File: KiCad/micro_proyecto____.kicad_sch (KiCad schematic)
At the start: 37 parts, among them J1 Conn_01x02, J2 Conn_01x05, J3 Conn_01x02, J4 Conn_01x02, J5 Conn_01x02, J6 Conn_01x02, SW1 SW_Push, SW2 SW_Push, SW3 SW_Push, SW4 SW_Push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

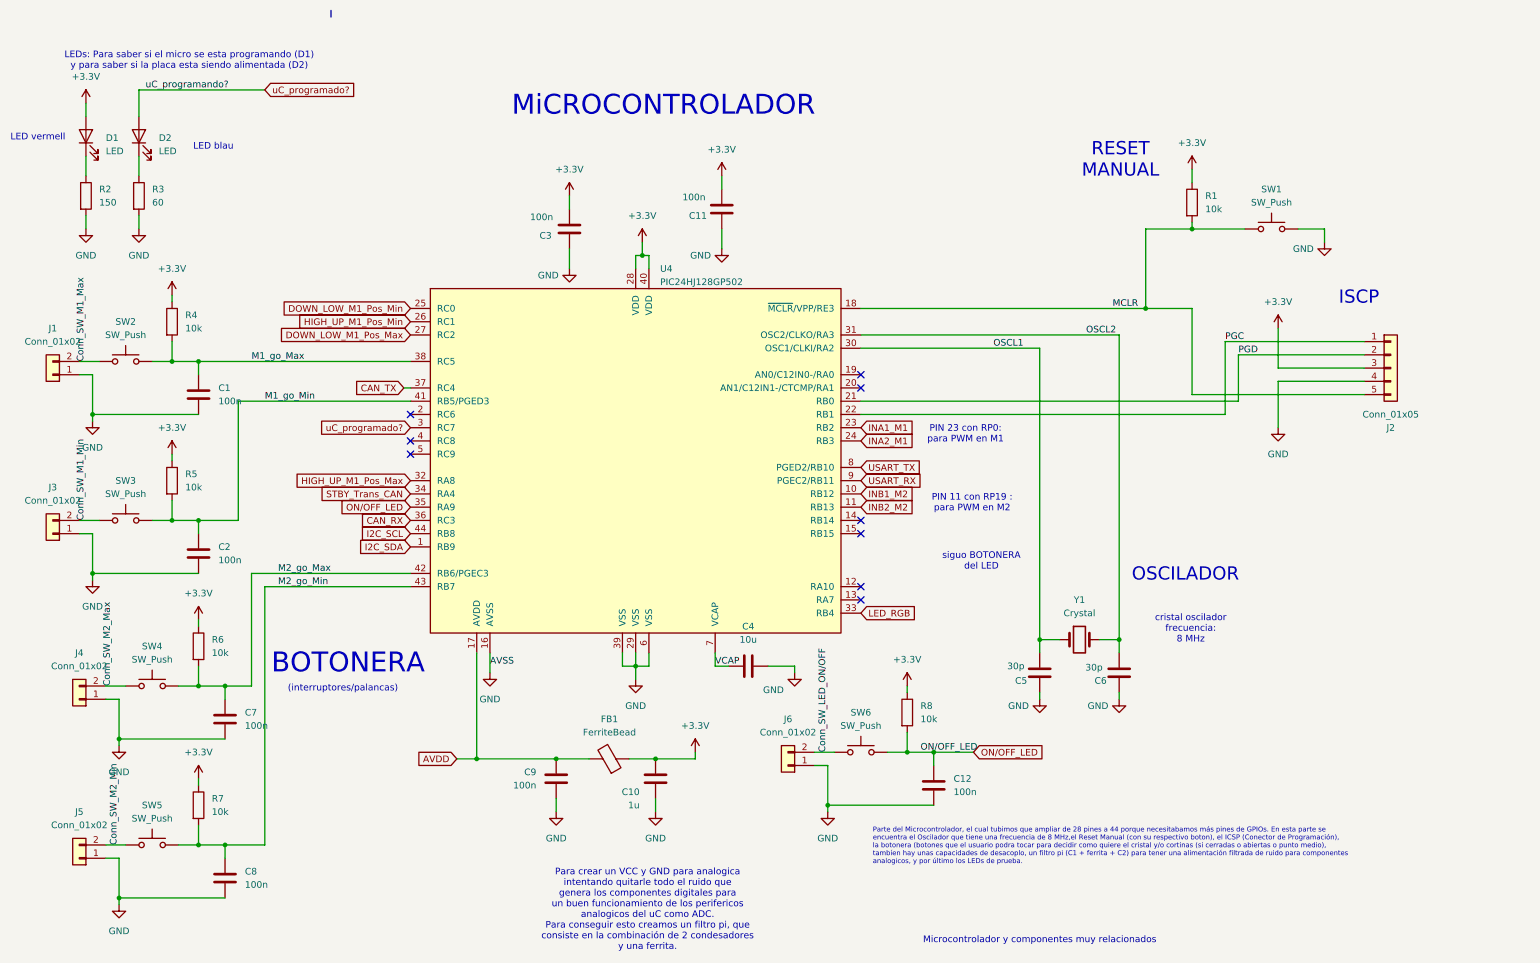
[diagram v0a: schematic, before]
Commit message: Layout con pocos cables en capa Bot pero todavai hay que hacer cambios que nos dijo el Miercoles pasado
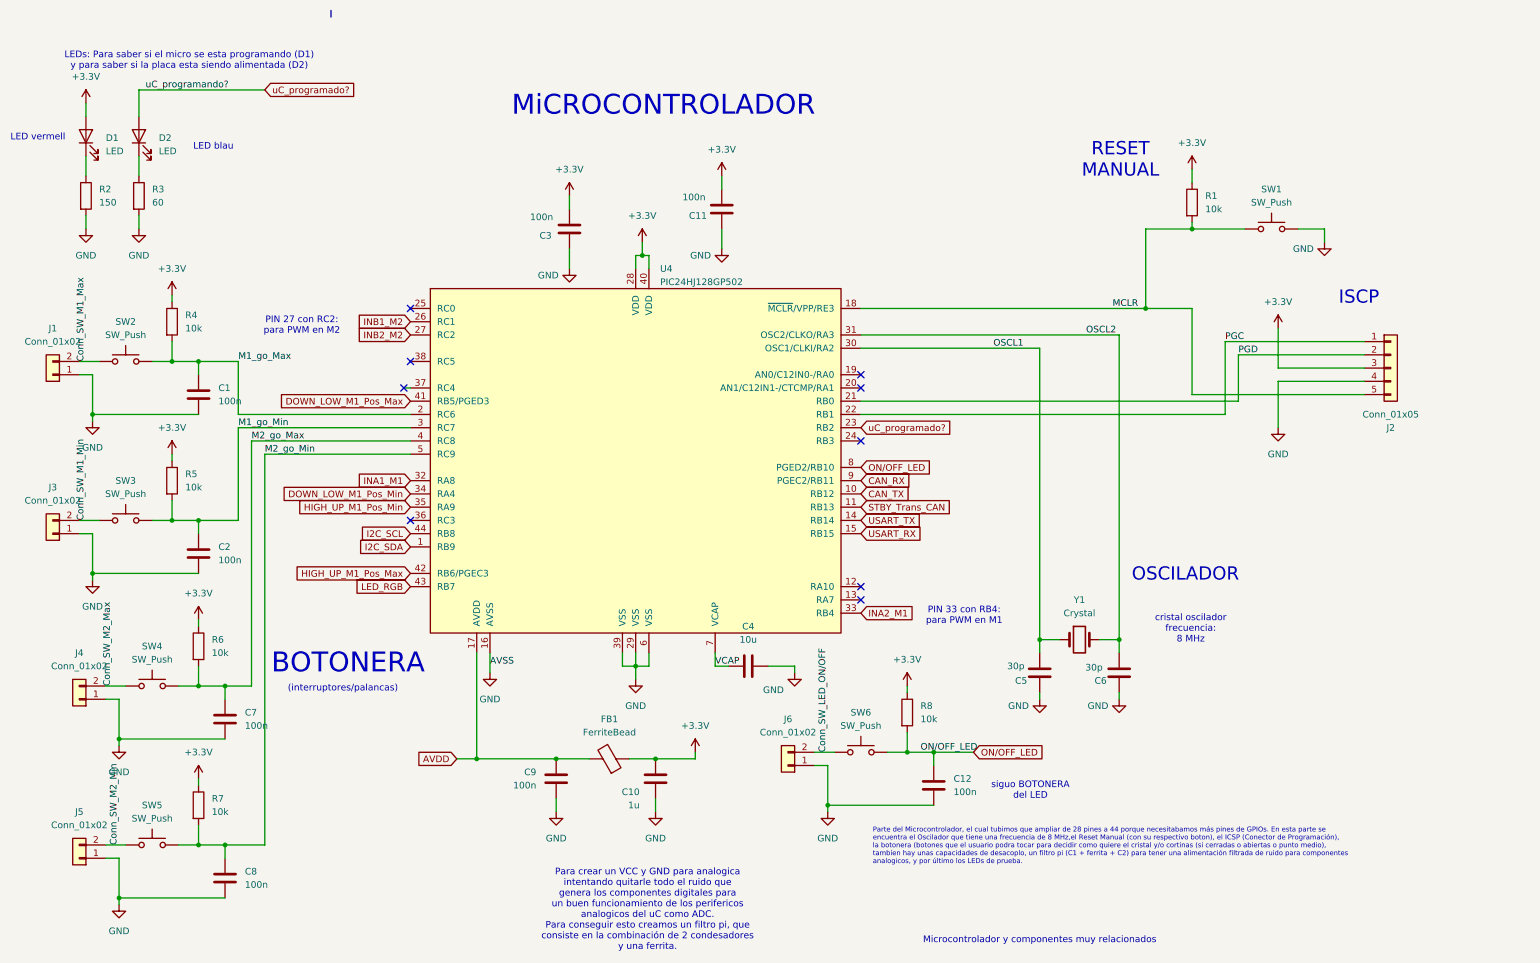
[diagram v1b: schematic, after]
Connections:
- net CAN_RX: now also U4.9 (PGEC2/RB11); no longer U4.36 (RC3)
- net CAN_TX: now also U4.10 (RB12); no longer U4.37 (RC4)
- net DOWN_LOW_M1_Pos_Max: now also U4.41 (RB5/PGED3); no longer U4.27 (RC2)
- net DOWN_LOW_M1_Pos_Min: now also U4.34 (NC); no longer U4.25 (RC0)
- net HIGH_UP_M1_Pos_Max: now also U4.42 (RB6/PGEC3); no longer U4.32 (RA8)
- net HIGH_UP_M1_Pos_Min: now also U4.35 (RA9); no longer U4.26 (RC1)
- net INA1_M1: now also U4.32 (RA8); no longer U4.23 (RB2)
- net INA2_M1: now also U4.33 (RB4); no longer U4.24 (RB3)
- net INB1_M2: now also U4.26 (RC1); no longer U4.10 (RB12)
- net INB2_M2: now also U4.27 (RC2); no longer U4.11 (RB13)
- net LED_RGB: now also U4.43 (RB7); no longer U4.33 (RB4)
- net M1_go_Max: now also U4.2 (RC6); no longer U4.38 (RC5)
- net M1_go_Min: now also U4.3 (RC7); no longer U4.41 (RB5/PGED3)
- net M2_go_Max: now also U4.4 (RC8); no longer U4.42 (RB6/PGEC3)
- net M2_go_Min: now also U4.5 (RC9); no longer U4.43 (RB7)
- net ON/OFF_LED: now also U4.8 (PGED2/RB10); no longer U4.35 (RA9)
- net STBY_Trans_CAN: now also U4.11 (RB13); no longer U4.34 (NC)
- net USART_RX: now also U4.15 (RB15); no longer U4.9 (PGEC2/RB11)
- net USART_TX: now also U4.14 (RB14); no longer U4.8 (PGED2/RB10)
- net uC_programado?: now also U4.23 (RB2); no longer U4.3 (RC7)
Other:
- note added: "PIN 27 con RC2: para PWM en M2"
- note added: "PIN 33 con RB4: para PWM en M1"
- note removed: "PIN 11 con RP19 : para PWM en M2"
- note removed: "PIN 23 con RP0: para PWM en M1"

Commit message: Cambios Layout propuestos para mejorar posicionamiento
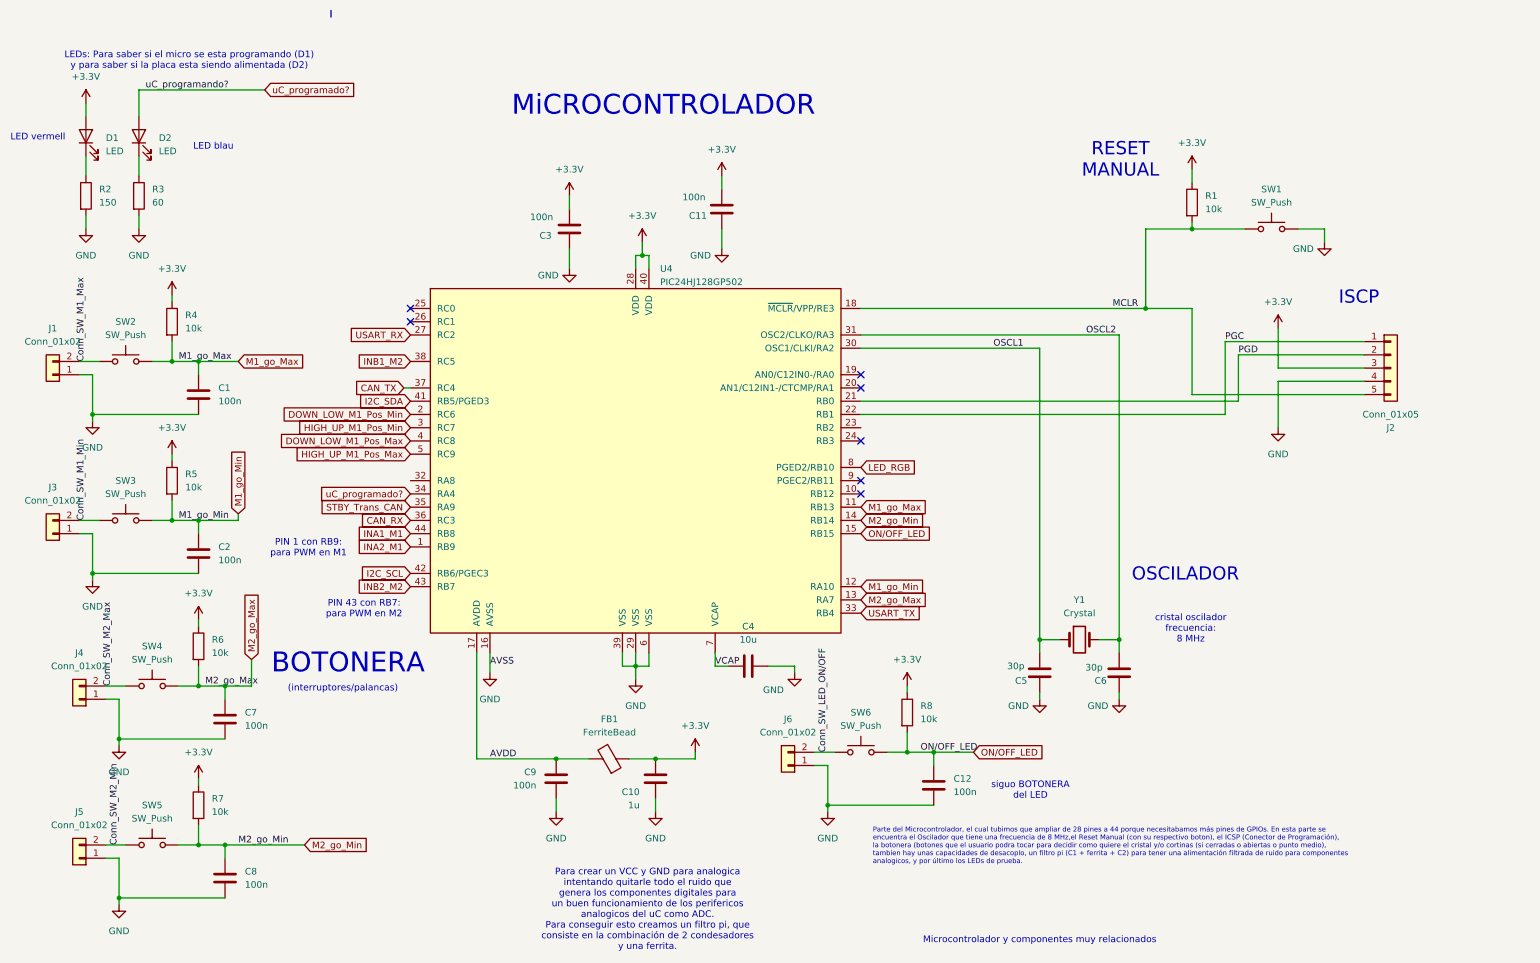
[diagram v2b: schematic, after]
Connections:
- net CAN_RX: now also U4.36 (RC3); no longer U4.9 (PGEC2/RB11)
- net CAN_TX: now also U4.37 (RC4); no longer U4.10 (RB12)
- net DOWN_LOW_M1_Pos_Max: now also U4.4 (RC8); no longer U4.41 (RB5/PGED3)
- net DOWN_LOW_M1_Pos_Min: now also U4.2 (RC6); no longer U4.34 (NC)
- net HIGH_UP_M1_Pos_Max: now also U4.5 (RC9); no longer U4.42 (RB6/PGEC3)
- net HIGH_UP_M1_Pos_Min: now also U4.3 (RC7); no longer U4.35 (RA9)
- net I2C_SCL: now also U4.42 (RB6/PGEC3); no longer U4.44 (RB8)
- net I2C_SDA: now also U4.41 (RB5/PGED3); no longer U4.1 (RB9)
- net INA1_M1: now also U4.44 (RB8); no longer U4.32 (RA8)
- net INA2_M1: now also U4.1 (RB9); no longer U4.33 (RB4)
- net INB1_M2: now also U4.38 (RC5); no longer U4.26 (RC1)
- net INB2_M2: now also U4.43 (RB7); no longer U4.27 (RC2)
- net LED_RGB: now also U4.8 (PGED2/RB10); no longer U4.43 (RB7)
- net M1_go_Max: now also U4.11 (RB13); no longer U4.2 (RC6)
- net M1_go_Min: now also U4.12 (RA10); no longer U4.3 (RC7)
- net M2_go_Max: now also U4.13 (RA7); no longer U4.4 (RC8)
- net M2_go_Min: now also U4.14 (RB14); no longer U4.5 (RC9)
- net ON/OFF_LED: now also U4.15 (RB15); no longer U4.8 (PGED2/RB10)
- net STBY_Trans_CAN: now also U4.35 (RA9); no longer U4.11 (RB13)
- net USART_RX: now also U4.27 (RC2); no longer U4.15 (RB15)
- net USART_TX: now also U4.33 (RB4); no longer U4.14 (RB14)
- net uC_programado?: now also U4.34 (NC); no longer U4.23 (RB2)
- no-connect marks 9 -> 7
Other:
- note added: "PIN 1 con RB9: para PWM en M1"
- note added: "PIN 43 con RB7: para PWM en M2"
- note removed: "PIN 27 con RC2: para PWM en M2"
- note removed: "PIN 33 con RB4: para PWM en M1"

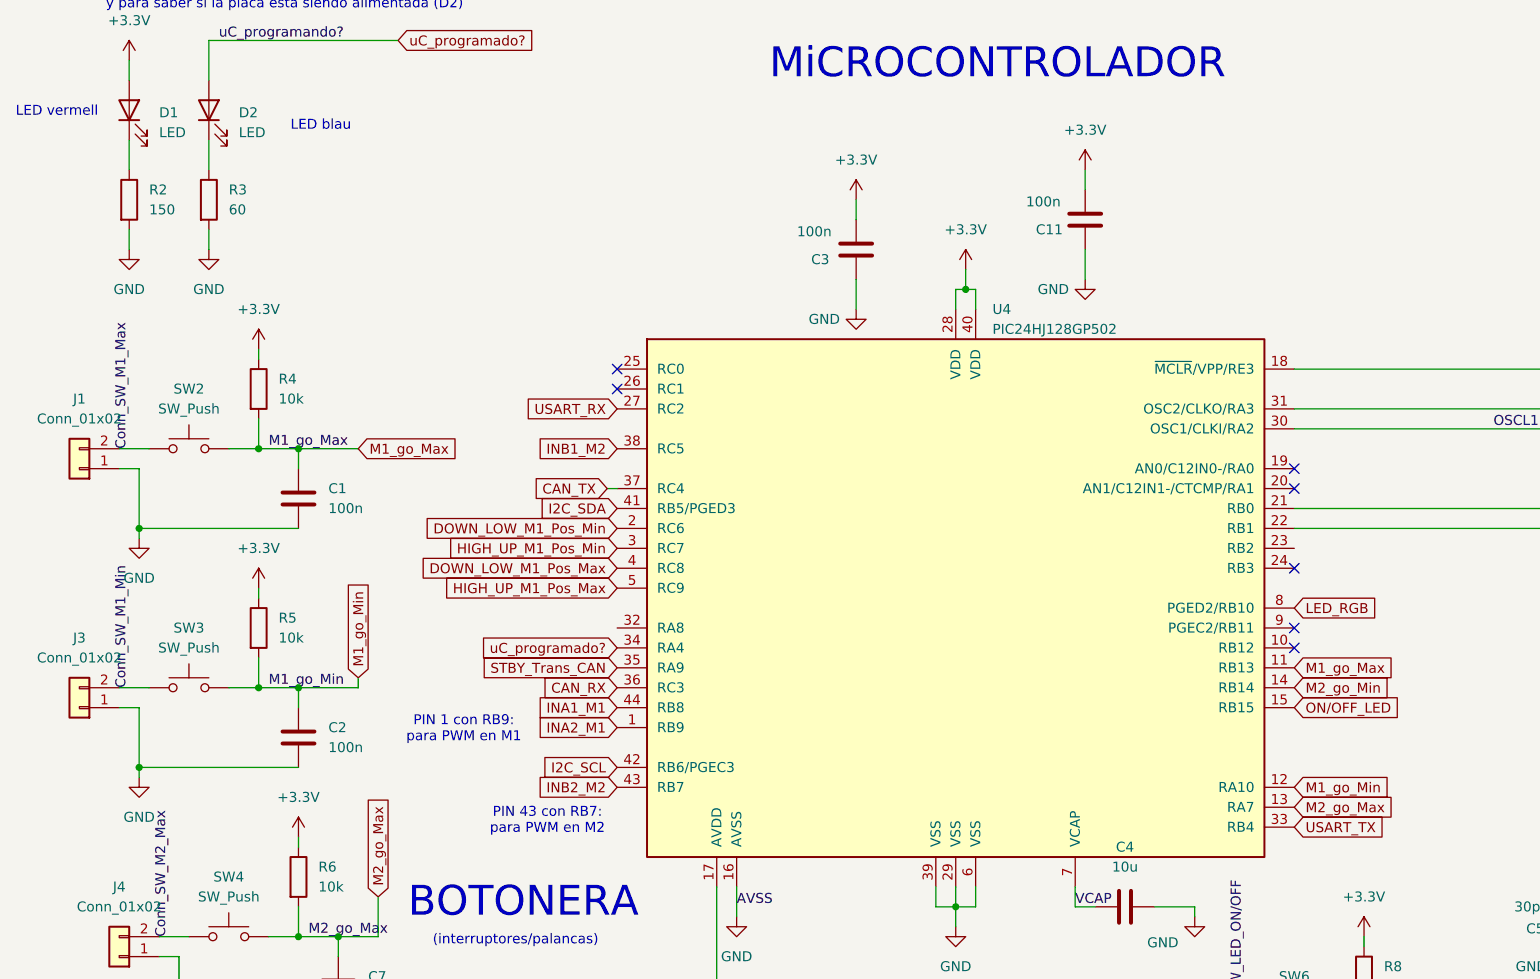
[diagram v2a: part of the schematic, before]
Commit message: Arreglo de algunos fallos DRC
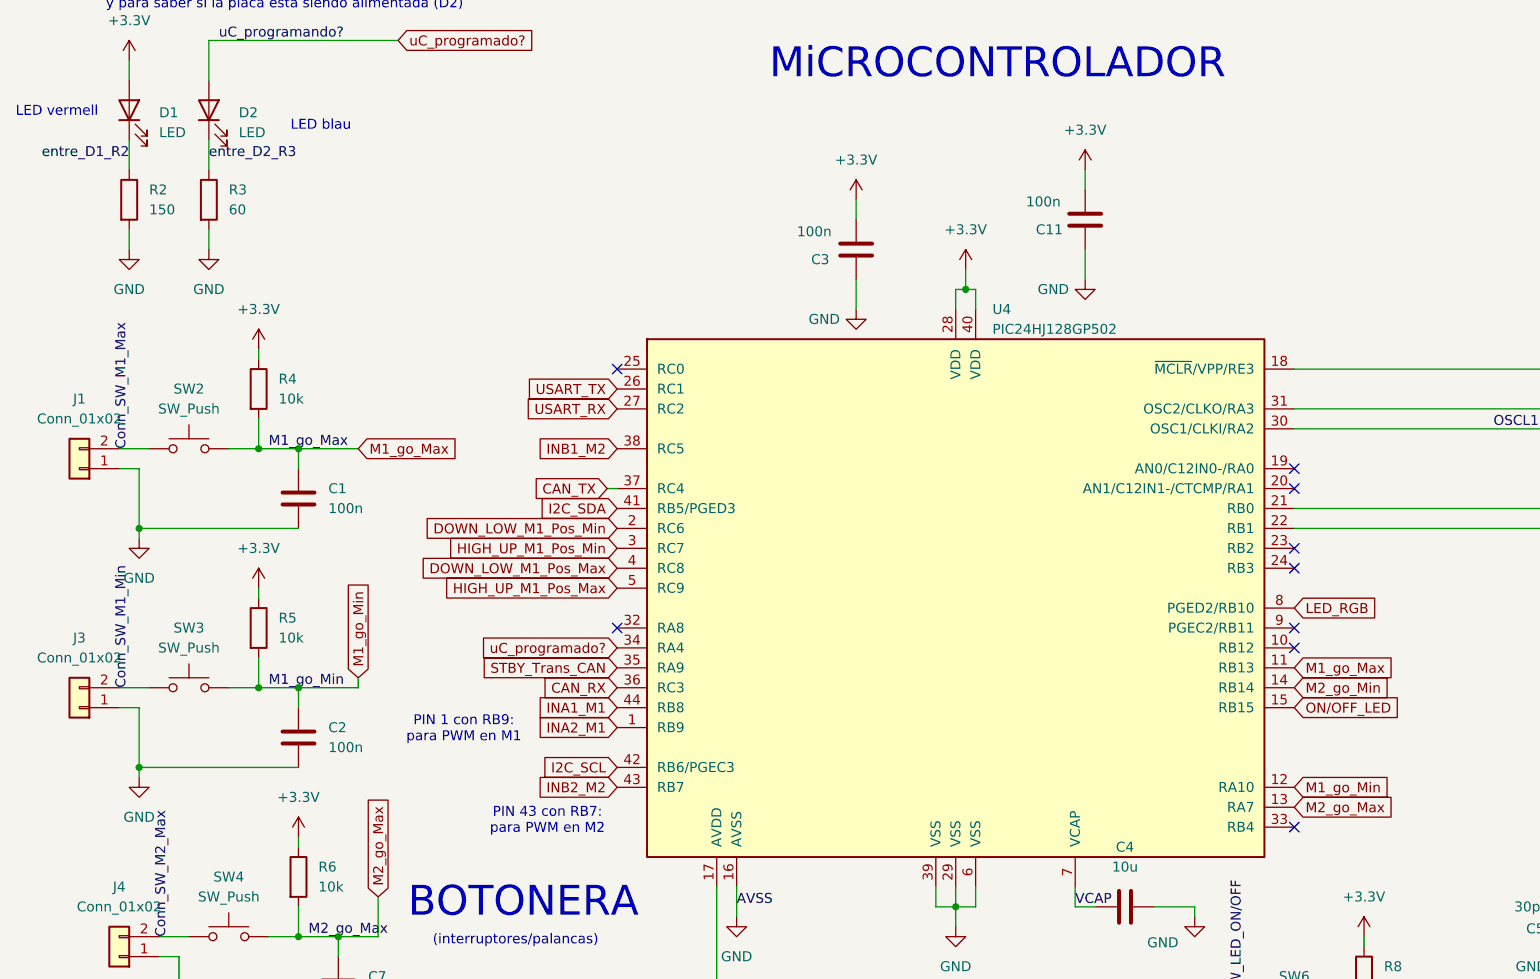
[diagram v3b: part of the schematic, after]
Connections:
- net USART_TX: now also U4.26 (RC1); no longer U4.33 (RB4)
- net entre_D2_R3: now reaches D2.1 (K), R3.1
- net entre_D1_R2: now reaches D1.1 (K), R2.1
- no-connect marks 7 -> 9
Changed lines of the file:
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@@
 	)
 	(no_connect
-		(at 90.17 71.12)
+		(at 176.53 91.44)
 	)
 	(no_connect
@@
 	)
 	(no_connect
+		(at 90.17 101.6)
+	)
+	(no_connect
+		(at 176.53 127)
+	)
+	(no_connect
 		(at 176.53 93.98)
 	)
@@
 		)
 	)
+	(label "entre_D2_R3"
+		(at 38.1 41.91 0)
+		(effects
+			(font
+				(size 1.27 1.27)
+			)
+			(justify left bottom)
+		)
+	)
 	(label "VCAP"
 		(at 148.59 137.16 0)
@@
 		)
 	)
+	(label "entre_D1_R2"
+		(at 27.94 41.91 180)
+		(effects
+			(font
+				(size 1.27 1.27)
+			)
+			(justify right bottom)
+		)
+	)
 	(label "ON{slash}OFF_LED"
 		(at 187.96 153.67 0)
@@
 	(global_label "USART_TX"
 		(shape input)
-		(at 176.53 127 0)
-		(fields_autoplaced yes)
-		(effects
-			(font
-				(size 1.27 1.27)
-			)
-			(justify left)
-		)
-		(property "Intersheetrefs" "${INTERSHEET_REFS}"
-			(at 188.5261 127 0)
-			(effects
-				(font
-					(size 1.27 1.27)
-				)
-				(justify left)
-				(hide yes)
-			)
+		(at 90.17 71.12 180)
+		(fields_autoplaced yes)
+		(effects
+			(font
+				(size 1.27 1.27)
+			)
+			(justify right)
+		)
+		(property "Intersheetrefs" "${INTERSHEET_REFS}"
+			(at 78.1739 71.12 0)
+			(effects
+				(font
+					(size 1.27 1.27)
+				)
+				(justify right)
+				(hide yes)
+			)
